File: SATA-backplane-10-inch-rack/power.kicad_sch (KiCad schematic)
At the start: 7 parts, among them J201 Barrel_Jack_Switch_Pin3Ring, U201 HW-613 5V0, U202 HW-613 3V3

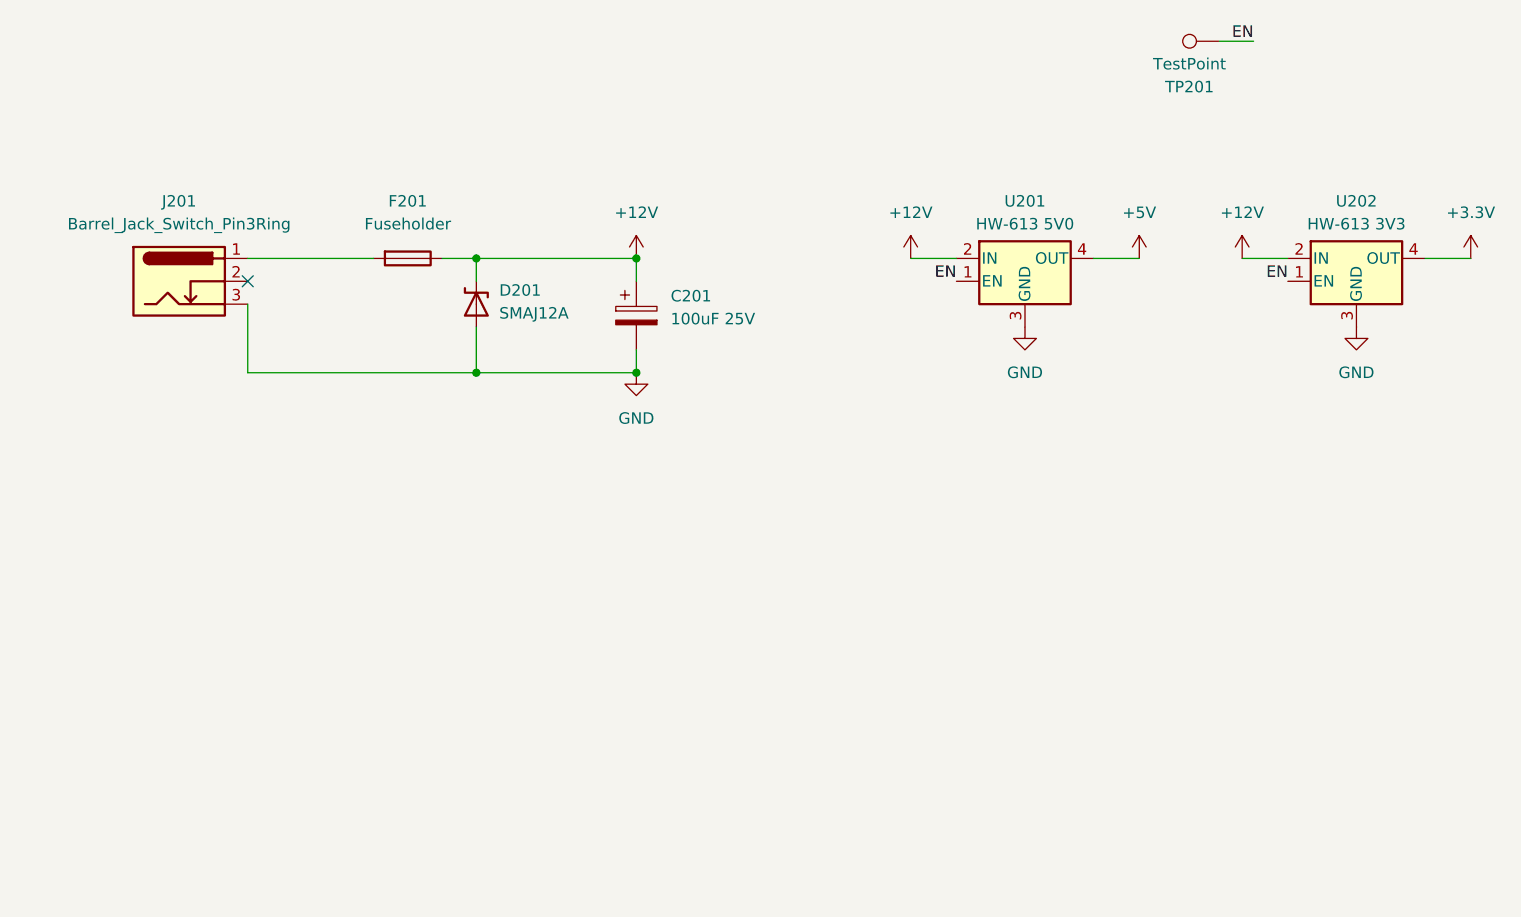
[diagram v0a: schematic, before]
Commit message: More realistic layout
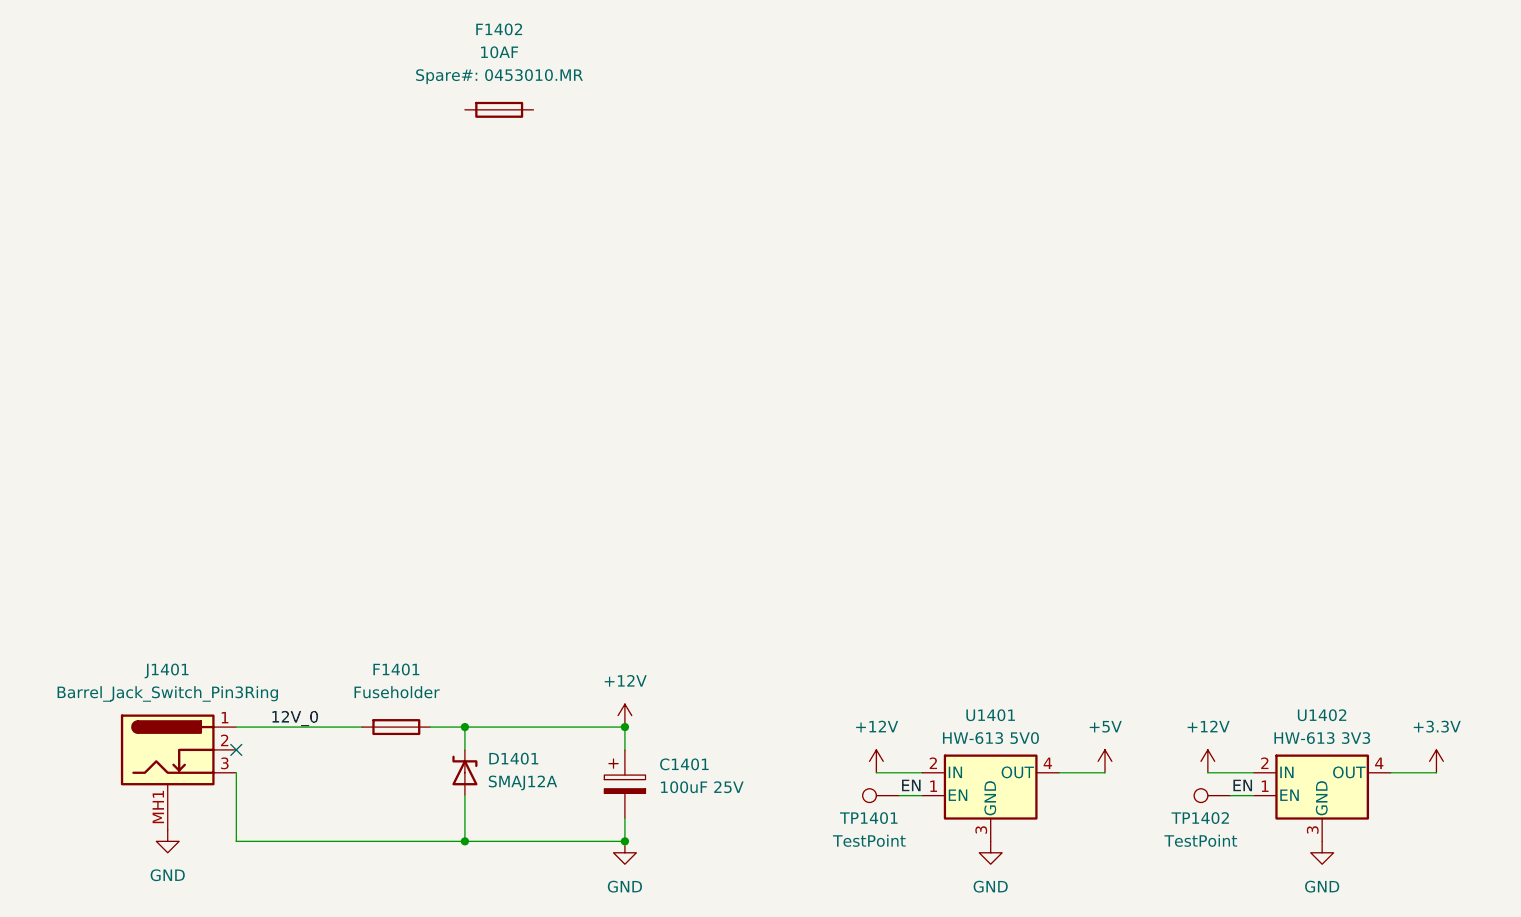
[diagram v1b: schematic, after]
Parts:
- removed C201: 100uF 25V, Capacitor_SMD:CP_Elec_8x10.5, symbol Device:C_Polarized
- removed D201: SMAJ12A, Diode_SMD:D_SMA-SMB_Universal_Handsoldering, symbol Kharars-KiCAD-lib:D_TVS_UNI
- removed F201: Fuseholder, Libraries:Fuseholder_Cylinder-5x20mm_Wuerth_696103101002-SMD_Horizontal_Open, symbol Device:Fuse
- removed J201: Barrel_Jack_Switch_Pin3Ring, Libraries:PJ036AHSMTTR, symbol Connector:Barrel_Jack_Switch_Pin3Ring
- removed TP201: TestPoint, TestPoint:TestPoint_Pad_D3.0mm, symbol Connector:TestPoint
- removed U201: HW-613 5V0, Connector_PinHeader_2.54mm:PinHeader_1x04_P2.54mm_Vertical_SMD_Pin1Right, symbol HW-613:HW-613
- removed U202: HW-613 3V3, Connector_PinHeader_2.54mm:PinHeader_1x04_P2.54mm_Vertical_SMD_Pin1Right, symbol HW-613:HW-613
- added C1401: 100uF 25V, Capacitor_SMD:CP_Elec_8x10.5, symbol Device:C_Polarized
- added D1401: SMAJ12A, Diode_SMD:D_SMA-SMB_Universal_Handsoldering, symbol Kharars-KiCAD-lib:D_TVS_UNI
- added F1401: Fuseholder, Libraries:Fuseholder_Cylinder-5x20mm_Wuerth_696103101002-SMD_Horizontal_Open, symbol Device:Fuse
- added F1402: 10AF, Kharars-KiCAD-lib:Fuse_Littlefuse-154_holder, symbol Device:Fuse
- added J1401: Barrel_Jack_Switch_Pin3Ring, Libraries:DCJ25015AK1C, symbol DCJ250-15-A-K1-C:Barrel_Jack_Switch_Pin3Ring
- added TP1401, TP1402: TestPoint, TestPoint:TestPoint_Pad_D1.5mm, symbol Connector:TestPoint
- added U1401: HW-613 5V0, Libraries:HW-613, symbol HW-613:HW-613
- added U1402: HW-613 3V3, Libraries:HW-613, symbol HW-613:HW-613
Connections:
- net +12V: now also C1401.1, D1401.1 (A1), F1401.1, U1401.2 (IN), U1402.2 (IN)
- net +3.3V: now also U1402.4 (OUT)
- net +5V: now also U1401.4 (OUT)
- net EN: now also TP1401.1, TP1402.1, U1401.1 (EN), U1402.1 (EN)
- net GND: now also C1401.2, D1401.2 (A2), J1401.3, J1401.MH1, U1401.3 (GND), U1402.3 (GND)
- new net 12V_0: F1401.2, J1401.1
